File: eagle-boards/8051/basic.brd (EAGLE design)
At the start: 59.4 x 48.2 mm, 12 parts, among them IC1 AT89S51-24P, Q1 12M

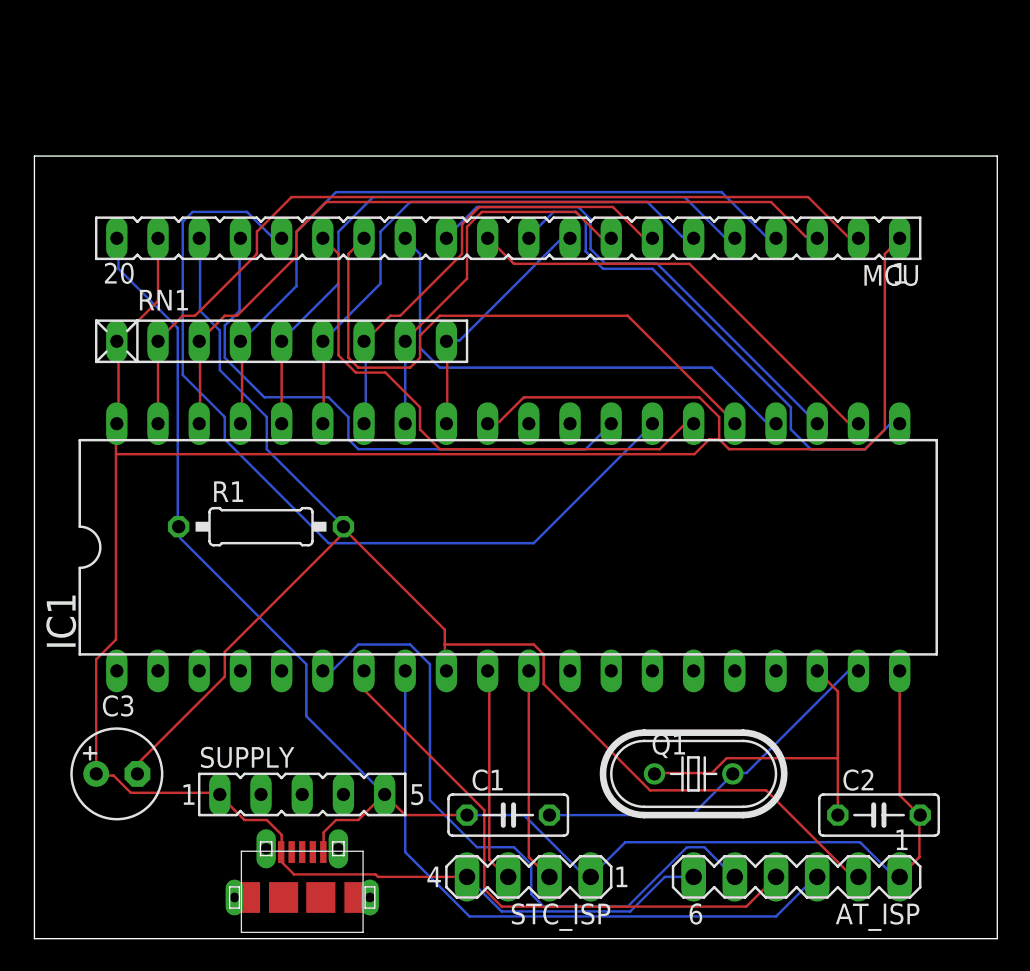
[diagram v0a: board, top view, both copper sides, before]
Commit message: New revision for the STC89C52 controller board.
Include (optional) CP2104 USB-to-UART adapter to make it easier to program the board in-system.

Include a latching pushbutton for power, which is also needed to work correctly for in-system programming.
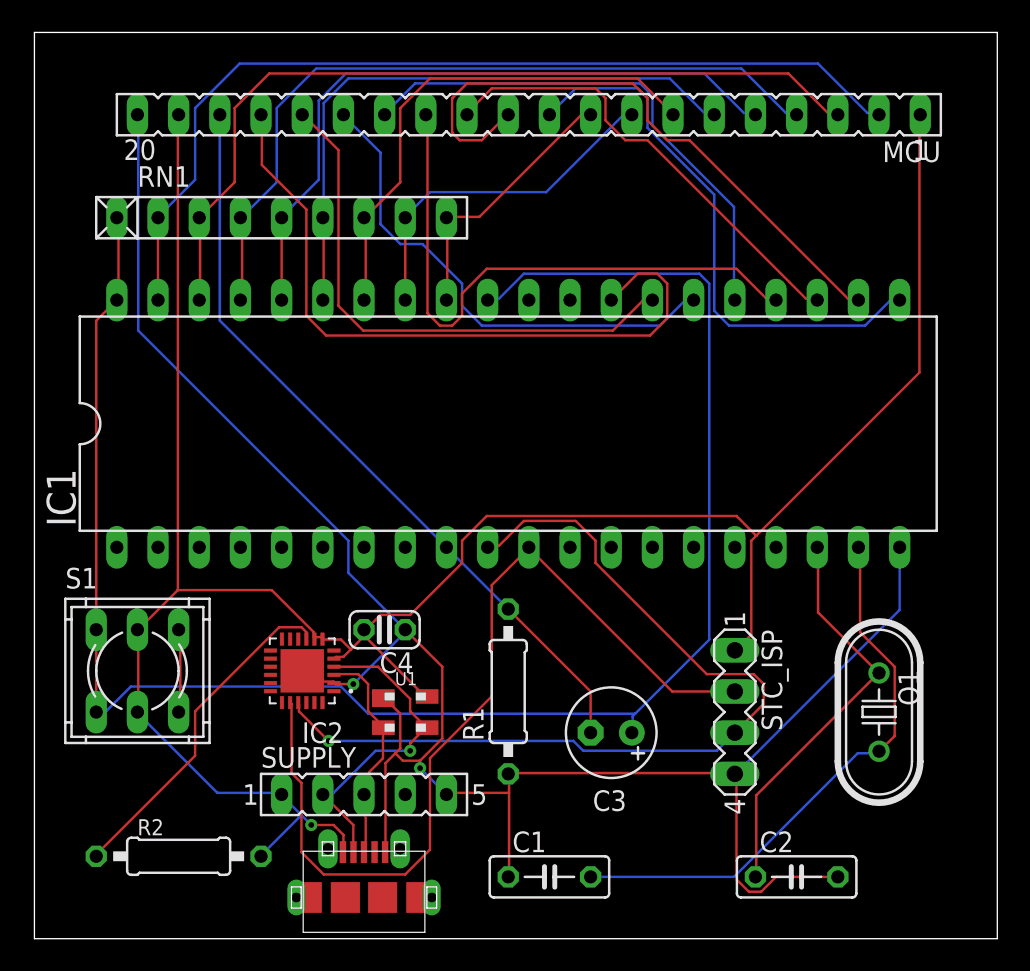
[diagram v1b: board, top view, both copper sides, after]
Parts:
- removed AT_ISP: (no value), con-lstb:MA06-1
- added C4: 1uF, rcl:C025-024X044
- added IC2: CP2104-F03-GM, CP2104:QFN50P400X400X80-25N
- added R2: 4.7k, rcl:0207/10
- added S1: 9077-2, switch-misc:9077-2
- added U1: SP0503BAHT, SP0503BAHT:SOT143
- moved C3 30.6 mm to (35.6, 12.7), turned to 180 degrees
- moved R1 18.3 mm to (29.2, 15.2), turned to 90 degrees
- moved STC_ISP 16.3 mm to (43.2, 14.0), turned to 270 degrees
- moved Q1 12.0 mm to (52.1, 14.0), turned to 270 degrees
- moved MCU 7.73 mm to (30.5, 50.8)
- moved RN1 7.62 mm to (15.2, 44.5)
- moved IC1 7.62 mm to (29.2, 31.8)
- moved C2 6.35 mm to (47.0, 3.81)
- moved C1 4.58 mm to (31.8, 3.81)
- moved SUPPLY 3.81 mm to (20.3, 8.89)
- moved U$1 3.81 mm to (20.3, 2.54)
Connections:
- removed net N$49: AT_ISP.3, IC1.8
- removed net N$50: AT_ISP.4, IC1.7
- removed net N$51: AT_ISP.5, IC1.6
- removed net VCC: AT_ISP.6, C3.+, IC1.31, IC1.40, MCU.1, MCU.19, RN1.1, STC_ISP.4, SUPPLY.1, U$1.1
- new net +5V: C4.2, IC2.5, IC2.7, IC2.8, MCU.1, MCU.19, R2.2, S1.2, S1.5, STC_ISP.1, SUPPLY.1, U$1.1, U1.4
- new net N$1: IC2.4, SUPPLY.2, U$1.2, U1.3
- new net N$20: IC2.3, SUPPLY.3, U$1.3, U1.2
- new net N$23: S1.3, S1.6
- new net N$24: IC2.9, R2.1
- new net N$27: C3.+, IC1.31, IC1.40, RN1.1, S1.1, S1.4
- new net VDD: IC2.6
- net GND: now also C4.1, IC2.2, IC2.25, STC_ISP.4, U1.1; no longer AT_ISP.1, STC_ISP.1
- net N$18: now also IC2.21
- net N$5: no longer AT_ISP.2
- net N$52: now also IC2.20
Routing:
- net VCC: track 154.6 -> 0.00 mm
- net +5V: track 0.00 -> 145.9 mm, vias 0 -> 1
- net N$27: track 0.00 -> 109.9 mm
- net N$52: track 13.3 -> 56.2 mm
- net N$18: track 13.3 -> 55.3 mm, vias 0 -> 1
- net N$51: track 41.0 -> 0.00 mm
- net N$49: track 39.2 -> 0.00 mm
- net N$5: track 86.1 -> 47.6 mm
- net N$50: track 35.7 -> 0.00 mm
- net GND: track 96.5 -> 127.2 mm, vias 0 -> 2
- net N$24: track 0.00 -> 21.0 mm
- net N$1: track 0.00 -> 20.5 mm, vias 0 -> 1
- net N$6: track 53.7 -> 33.5 mm
- net N$20: track 0.00 -> 13.7 mm
- net N$3: track 22.7 -> 34.9 mm
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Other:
- board size 59.4 x 48.2 mm -> 59.4 x 55.9 mm
- board text added: "Birch Books Smart Home - Controller Module STC89C52 rev. 3 Copyright © 2020 Diego Elio Pettenò flameeyes.com/p/birch-books Licensed under MIT License."
- board text removed: "Birch Books Smart Home Controller Module - AT89S52 rev. 1"

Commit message: Update components and layout for 8051 board.
Replace the microUSB connector to be the same Amphenol part as used in the ATmega board.

Replace the single electrolytic with a ceramic capacitor, and match the footprint between that and the CP2104 one.
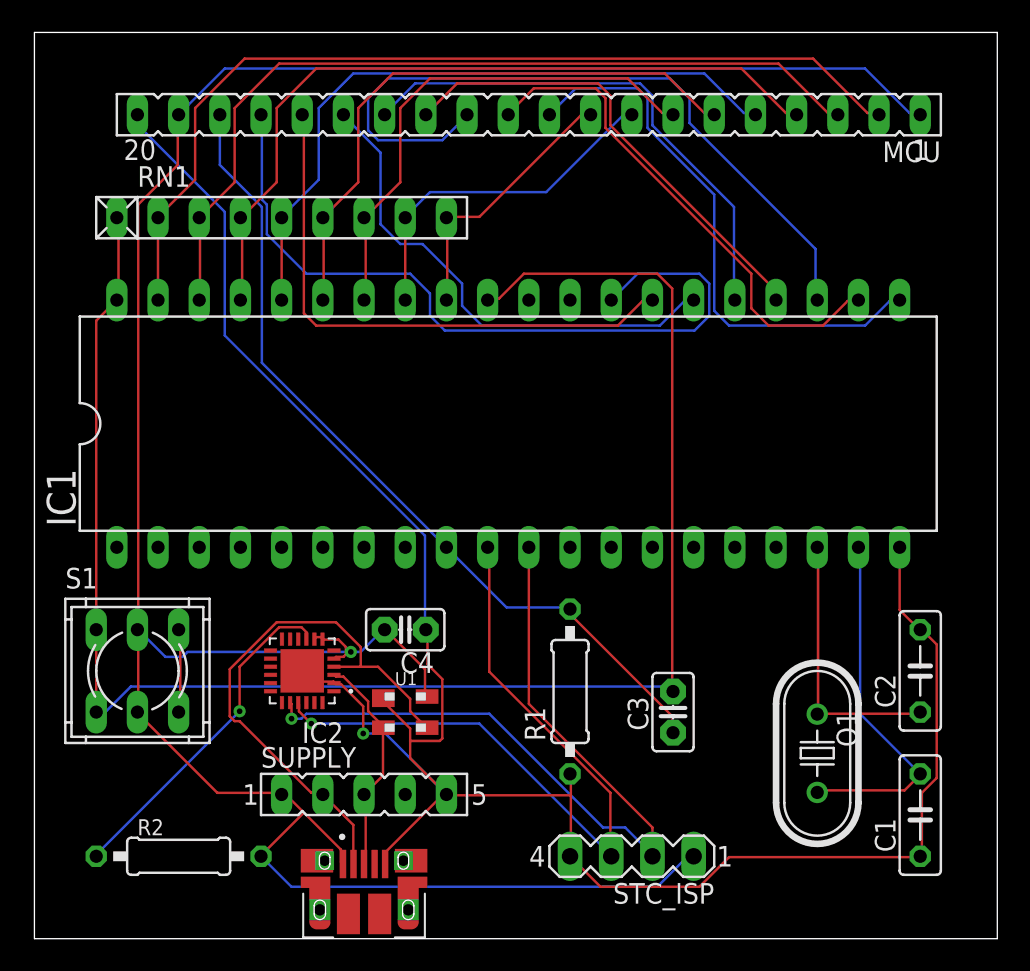
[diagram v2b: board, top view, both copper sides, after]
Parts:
- C3: device rcl:E2,5-6 -> capacitor-wima:C2.5-2
- C4: device rcl:C025-024X044 -> capacitor-wima:C2.5-2
- U$1: value MICRO-USB-RECEPTACLE47589-0001 -> 10103594-0001LF; device con-molex-usb:47589-0001 -> 10103594-0001LF:FCI_10103594-0001LF
- moved C1 23.2 mm to (54.6, 7.62), turned to 90 degrees
- moved C2 14.8 mm to (54.6, 16.5), turned to 270 degrees
- moved STC_ISP 10.9 mm to (36.8, 5.08), turned to 180 degrees
- moved Q1 4.58 mm to (48.3, 11.4)
- moved C3 4.02 mm to (39.4, 14.0), turned to 270 degrees
- moved R1 3.81 mm to (33.0, 15.2)
- moved C4 1.27 mm to (22.9, 19.1)
- moved U$1 0.76 mm to (20.3, 1.78), turned to 0 degrees
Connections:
- net N$27: now also C3.1; no longer C3.+
- net N$5: now also C3.2; no longer C3.-
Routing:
- net N$16: track 28.5 -> 45.5 mm
- net +5V: track 145.9 -> 160.9 mm
- net N$1: track 20.5 -> 34.6 mm, vias 1 -> 0
- net N$3: track 34.9 -> 22.4 mm
- net N$18: track 55.3 -> 45.7 mm
- net N$4: track 25.1 -> 16.7 mm
- net N$15: track 37.2 -> 29.3 mm
- net N$17: track 38.2 -> 31.3 mm
- net N$52: track 56.2 -> 49.3 mm, vias 0 -> 1
- net N$27: track 109.9 -> 104.8 mm
- net N$5: track 47.6 -> 51.9 mm
- net GND: track 127.2 -> 131.4 mm, vias 2 -> 1
- net N$2: track 43.3 -> 47.4 mm
- net N$6: track 33.5 -> 34.8 mm
- net N$11: track 37.9 -> 36.7 mm
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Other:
- board text added: "Birch Books Smart Home - Controller Module STC89C52 rev. 3a Copyright © 2020 Diego Elio Pettenò flameeyes.com/p/birch-books Licensed under MIT License."
- board text removed: "Birch Books Smart Home - Controller Module STC89C52 rev. 3 Copyright © 2020 Diego Elio Pettenò flameeyes.com/p/birch-books Licensed under MIT License."

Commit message: Replace the wima capacitor object with a generic one.
This is pretty much the same footprint (except the solder pad is slightly thinner), but it requires one less library, since the xtal's capacitors are coming from rcl as well.
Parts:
- C3, C4: device capacitor-wima:C2.5-2 -> rcl:C025-025X050
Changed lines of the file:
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@@
 <attribute name="VALUE" x="57.404" y="14.224" size="1.27" layer="27" ratio="10" rot="R90"/>
 </element>
-<element name="C3" library="capacitor-wima" library_urn="urn:adsk.eagle:library:116" package="C2.5-2" package3d_urn="urn:adsk.eagle:package:5415/1" value="10uF" x="39.37" y="13.97" smashed="yes" rot="R270">
+<element name="C3" library="rcl" library_urn="urn:adsk.eagle:library:334" package="C025-025X050" package3d_urn="urn:adsk.eagle:package:23629/2" value="10uF" x="39.37" y="13.97" smashed="yes" rot="R270">
 <attribute name="NAME" x="37.846" y="12.827" size="1.27" layer="25" ratio="10" rot="R90"/>
-<attribute name="POPULARITY" value="28" x="-11.43" y="-11.43" size="1.778" layer="27" rot="R270" display="off"/>
+<attribute name="POPULARITY" value="65" x="-11.43" y="-11.43" size="1.778" layer="27" rot="R270" display="off"/>
+<attribute name="SPICEPREFIX" value="C" x="39.37" y="13.97" size="1.778" layer="27" rot="R270" display="off"/>
 <attribute name="VALUE" x="42.037" y="11.557" size="1.27" layer="27" ratio="10" rot="R90"/>
 </element>
@@
 <attribute name="VALUE" x="7.2644" y="4.5974" size="0.9906" layer="27" ratio="10"/>
 </element>
-<element name="C4" library="capacitor-wima" library_urn="urn:adsk.eagle:library:116" package="C2.5-2" package3d_urn="urn:adsk.eagle:package:5415/1" value="1uF" x="22.86" y="19.05" smashed="yes" rot="R180">
+<element name="C4" library="rcl" library_urn="urn:adsk.eagle:library:334" package="C025-025X050" package3d_urn="urn:adsk.eagle:package:23629/2" value="1uF" x="22.86" y="19.05" smashed="yes" rot="R180">
 <attribute name="NAME" x="24.638" y="17.653" size="1.27" layer="25" ratio="10" rot="R180"/>
-<attribute name="POPULARITY" value="28" x="22.86" y="19.05" size="1.778" layer="27" rot="R180" display="off"/>
+<attribute name="POPULARITY" value="65" x="22.86" y="19.05" size="1.778" layer="27" rot="R180" display="off"/>
+<attribute name="SPICEPREFIX" value="C" x="22.86" y="19.05" size="1.778" layer="27" rot="R180" display="off"/>
 <attribute name="VALUE" x="24.638" y="21.717" size="1.27" layer="27" ratio="10" rot="R180"/>
 </element>
